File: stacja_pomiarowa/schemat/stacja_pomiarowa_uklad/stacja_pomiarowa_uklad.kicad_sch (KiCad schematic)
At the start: 24 parts, among them J1 Conn_02x17_Counter_Clockwise, J2 Conn_02x08_Counter_Clockwise, J3 Conn_01x01, J4 Conn_02x04_Counter_Clockwise, J5 Conn_01x02, J6 Conn_01x04, U1 CD4051B, U2 CD4051B, U3 ESP DevKitV1, U4 ADS1115, U5 CD4051B, U6 CD4051B, U7 MCP23017_SP, U8 4512

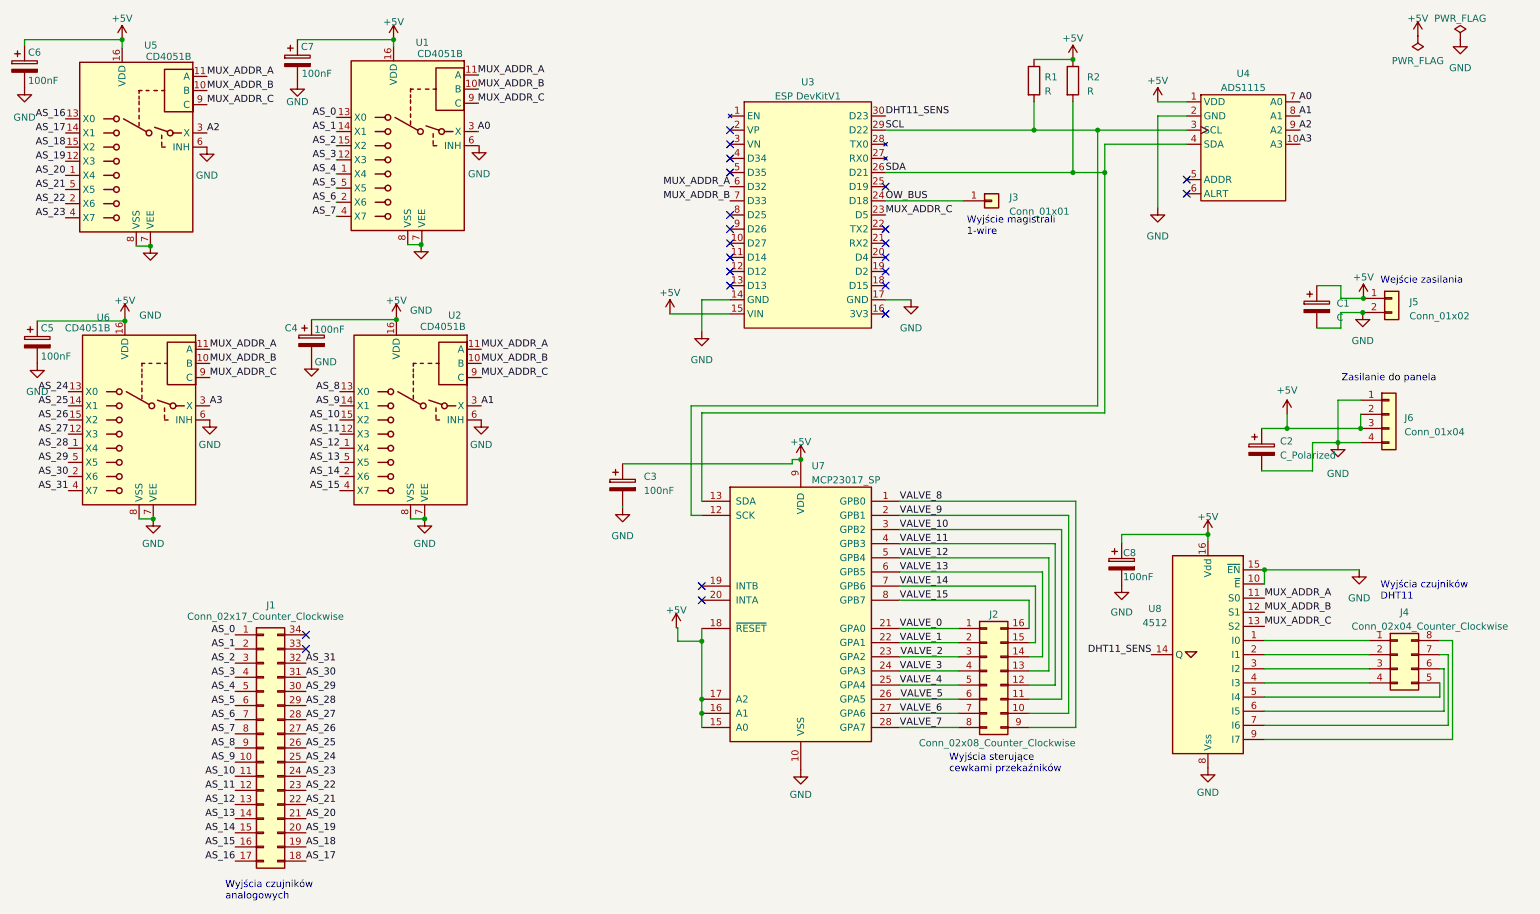
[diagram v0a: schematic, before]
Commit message: Poprawa schematu
Poprzednia numeracja wyjsc analogowych, dodany brakujacy tranzystor Q1, dodane brakujace oporniki podciagajace dla 1-wire i dht11, usuniete oporniki sciagajace dla wyjsc a[0..1] adc - w ten sposob przy niepodlaczonym czujniki nie bedzie stanu niskiego zamiast tego dodane oproniki sciagajace do zlacz dla czujnikow analogowych
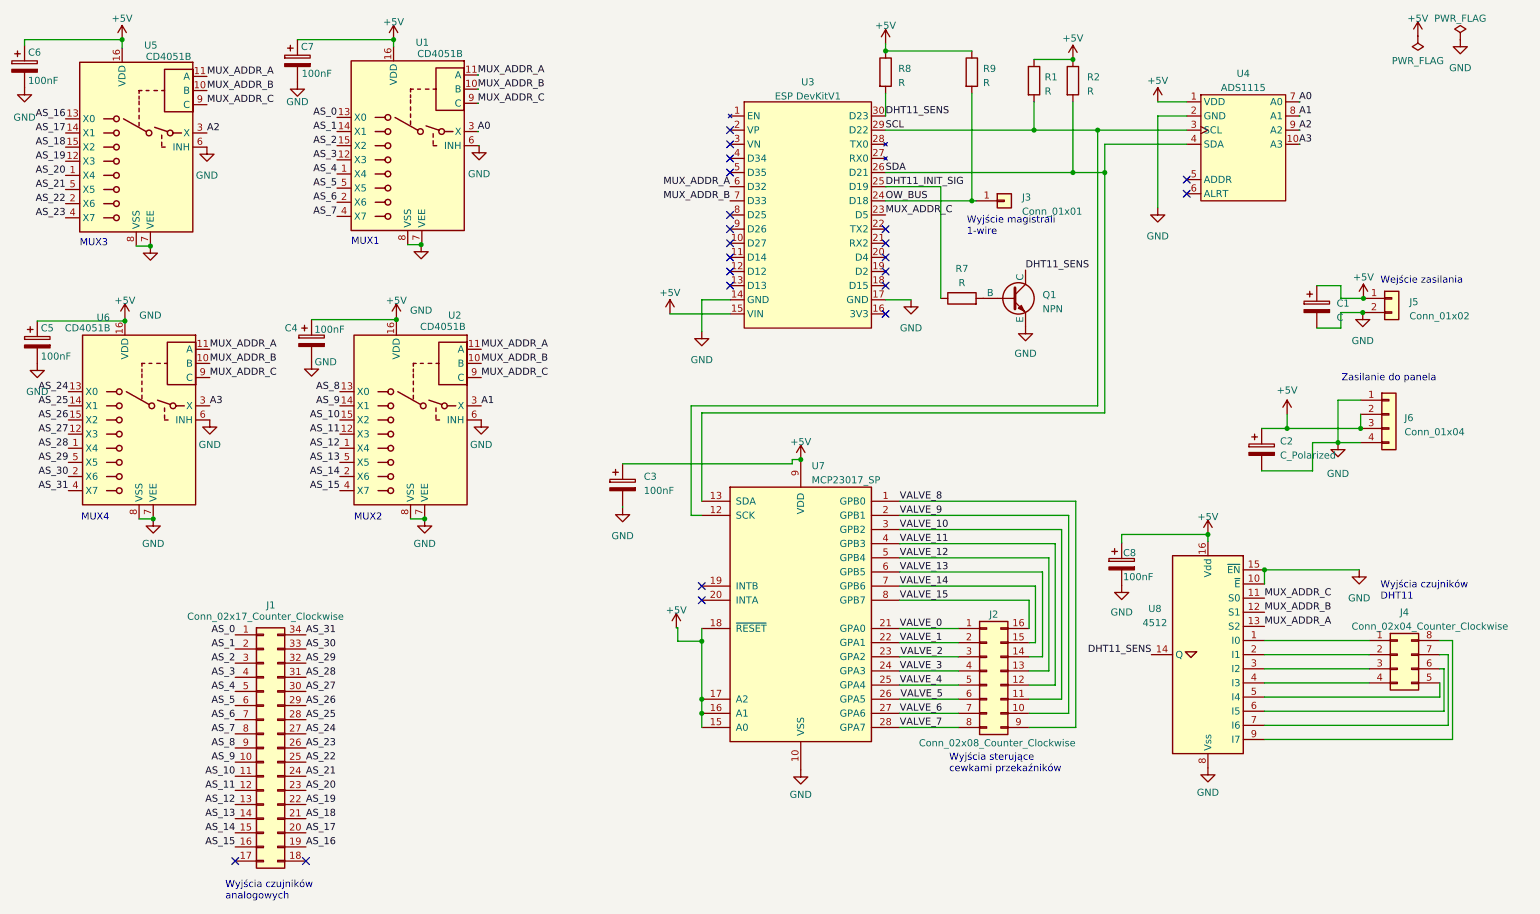
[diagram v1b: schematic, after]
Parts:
- added Q1: NPN, symbol Simulation_SPICE:NPN
- added R7, R8, R9: R, symbol Device:R
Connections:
- net +5V: now also R8.1, R9.1
- net AS_16: now also J1.19 (Pin_19); no longer J1.17 (Pin_17)
- net AS_17: now also J1.20 (Pin_20); no longer J1.18 (Pin_18)
- net AS_18: now also J1.21 (Pin_21); no longer J1.19 (Pin_19)
- net AS_19: now also J1.22 (Pin_22); no longer J1.20 (Pin_20)
- net AS_20: now also J1.23 (Pin_23); no longer J1.21 (Pin_21)
- net AS_21: now also J1.24 (Pin_24); no longer J1.22 (Pin_22)
- net AS_22: now also J1.25 (Pin_25); no longer J1.23 (Pin_23)
- net AS_23: now also J1.26 (Pin_26); no longer J1.24 (Pin_24)
- net AS_24: now also J1.27 (Pin_27); no longer J1.25 (Pin_25)
- net AS_25: now also J1.28 (Pin_28); no longer J1.26 (Pin_26)
- net AS_26: now also J1.29 (Pin_29); no longer J1.27 (Pin_27)
- net AS_27: now also J1.30 (Pin_30); no longer J1.28 (Pin_28)
- net AS_28: now also J1.31 (Pin_31); no longer J1.29 (Pin_29)
- net AS_29: now also J1.32 (Pin_32); no longer J1.30 (Pin_30)
- net AS_30: now also J1.33 (Pin_33); no longer J1.31 (Pin_31)
- net AS_31: now also J1.34 (Pin_34); no longer J1.32 (Pin_32)
- net DHT11_SENS: now also Q1.1 (C), R8.2
- net GND: now also Q1.3 (E)
- net MUX_ADDR_A: now also U8.13 (S2); no longer U8.11 (S0)
- net MUX_ADDR_C: now also U8.11 (S0); no longer U8.13 (S2)
- net OW_BUS: now also R9.2
- net DHT11_INIT_SIG: now reaches U3.25 (D19)
- net DHT11_INIT_SIG: now also R7.1
- new net: Q1.2 (B), R7.2
- no-connect marks 23 -> 22
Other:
- note added: "MUX1"
- note added: "MUX2"
- note added: "MUX3"
- note added: "MUX4"
- moved on the sheet: J3

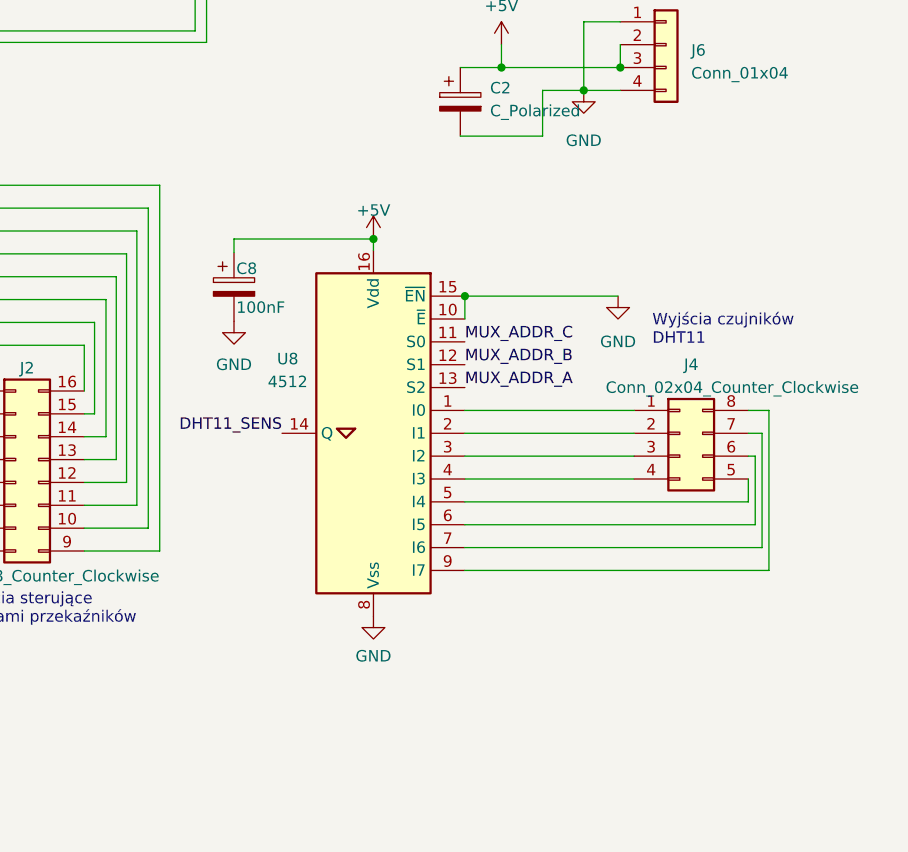
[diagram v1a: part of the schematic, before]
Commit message: Zmiana multipleksera 4512 na 4051
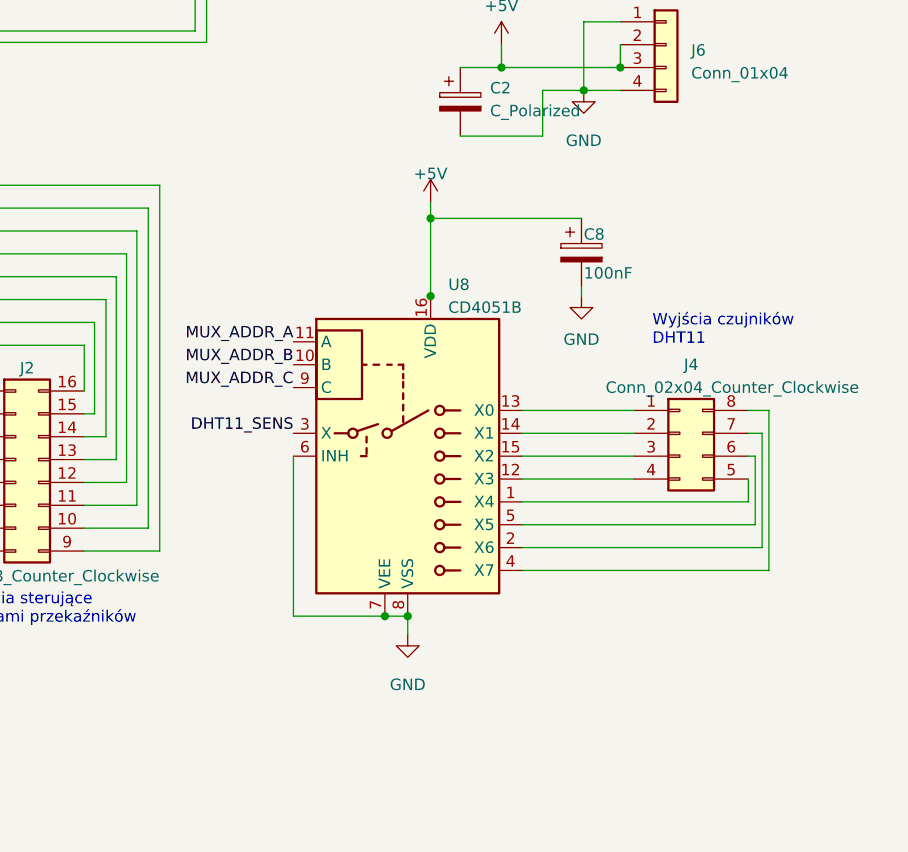
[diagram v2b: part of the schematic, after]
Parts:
- removed U8: 4512, Package_DIP:DIP-16_W7.62mm_Socket, symbol 4xxx_IEEE:4512
- added U8: CD4051B, symbol Analog_Switch:CD4051B
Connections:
- net +5V: now also U8.16 (VDD)
- net DHT11_SENS: now also U8.3 (X)
- net GND: now also U8.6 (INH), U8.7 (VEE), U8.8 (VSS)
- net MUX_ADDR_A: now also U8.11 (A)
- net MUX_ADDR_B: now also U8.10 (B)
- net MUX_ADDR_C: now also U8.9 (C)
- net at J4.1 (Pin_1): now also U8.13 (X0)
- net at J4.2 (Pin_2): now also U8.14 (X1)
- net at J4.3 (Pin_3): now also U8.15 (X2)
- net at J4.4 (Pin_4): now also U8.12 (X3)
- net at J4.5 (Pin_5): now also U8.1 (X4)
- net at J4.6 (Pin_6): now also U8.5 (X5)
- net at J4.7 (Pin_7): now also U8.2 (X6)
- net at J4.8 (Pin_8): now also U8.4 (X7)
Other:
- moved on the sheet: C8

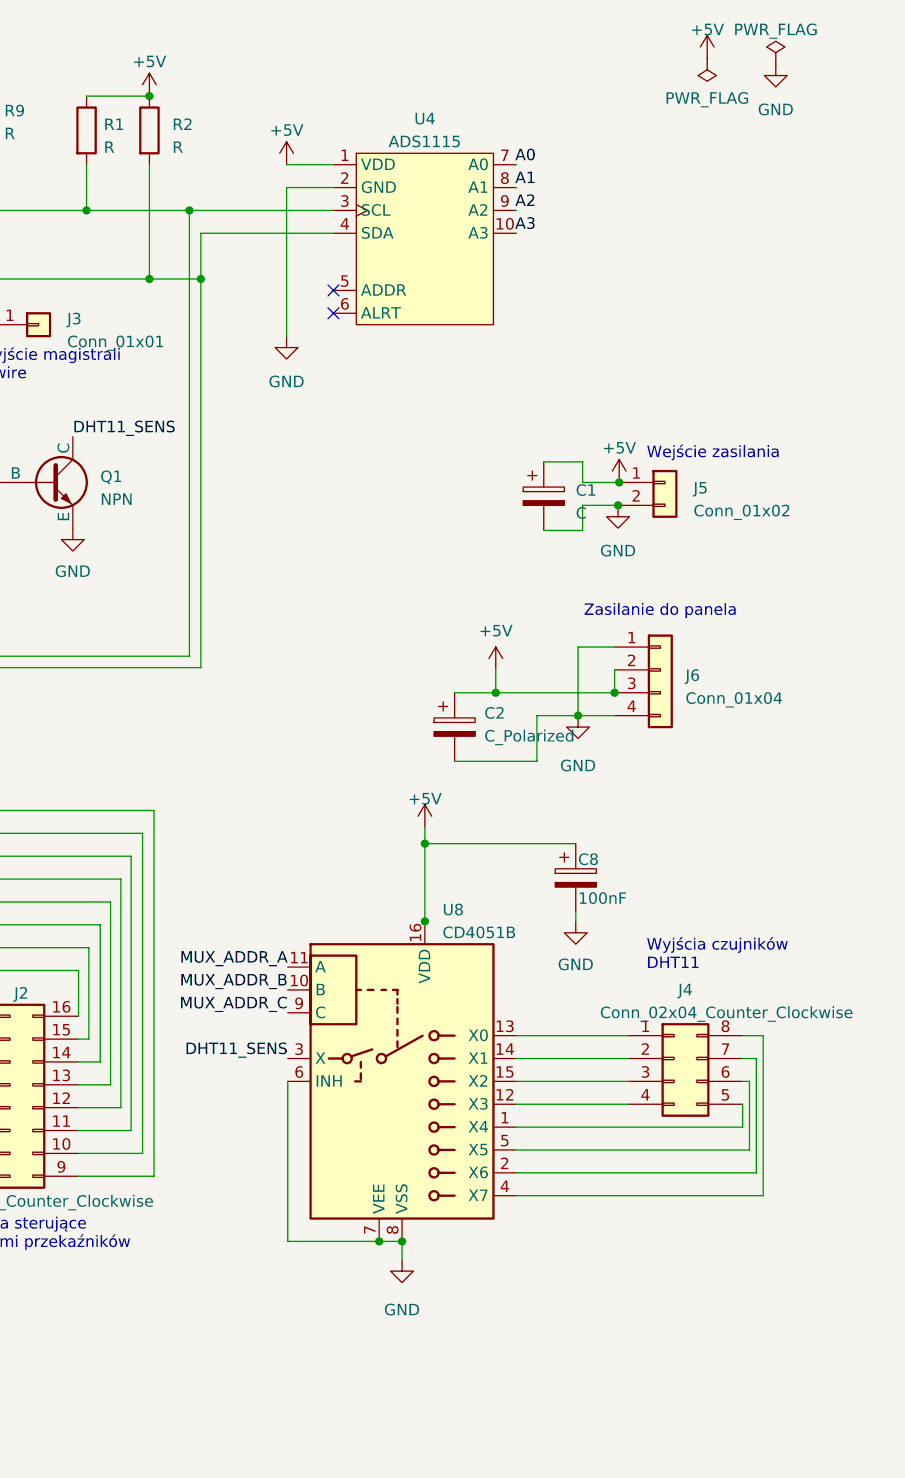
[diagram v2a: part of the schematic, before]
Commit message: Przywrócono oporniki do wejść ads1115, dodano brakujące oporniki do wejść multipleksera od dht11
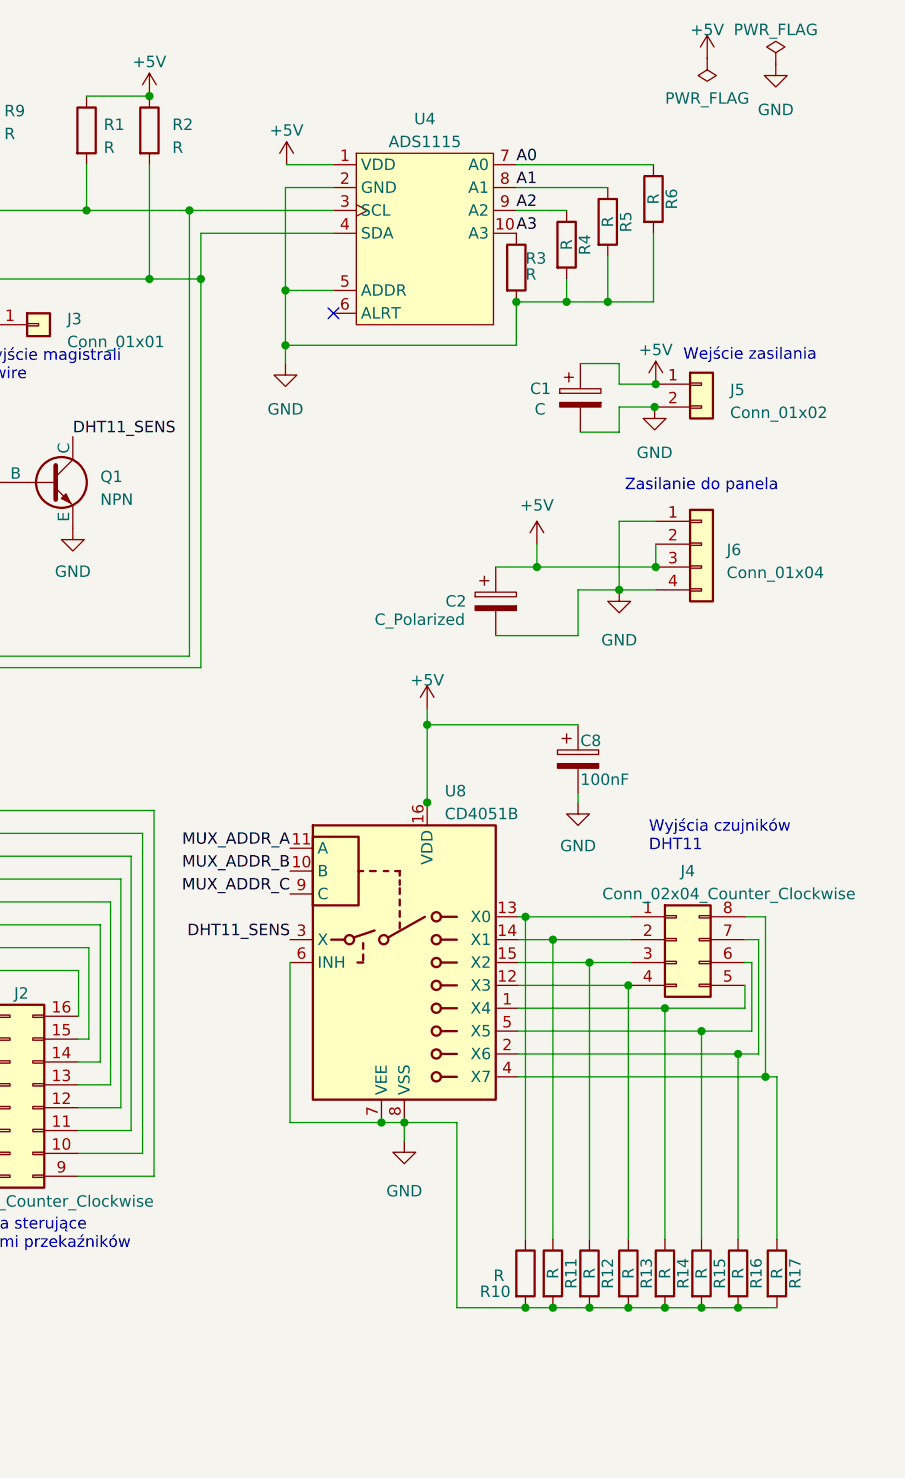
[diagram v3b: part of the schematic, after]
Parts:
- added R10, R11, R12, R13, R14, R15, R16, R17, R3, R4, R5, R6: R, symbol Device:R
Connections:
- net A0: now also R6.1
- net A1: now also R5.1
- net A2: now also R4.1
- net A3: now also R3.1
- net GND: now also U4.5 (ADDR), R10.2, R11.2, R12.2, R13.2, R14.2, R15.2, R16.2, R17.2, R3.2, R4.2, R5.2, R6.2
- net at J4.1 (Pin_1), U8.13 (X0): now also R10.1
- net at J4.2 (Pin_2), U8.14 (X1): now also R11.1
- net at J4.3 (Pin_3), U8.15 (X2): now also R12.1
- net at J4.4 (Pin_4), U8.12 (X3): now also R13.1
- net at J4.5 (Pin_5), U8.1 (X4): now also R14.1
- net at J4.6 (Pin_6), U8.5 (X5): now also R15.1
- net at J4.7 (Pin_7), U8.2 (X6): now also R16.1
- net at J4.8 (Pin_8), U8.4 (X7): now also R17.1
- no-connect marks 22 -> 21
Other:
- moved on the sheet: C1, C2, C8, J4, J5, J6, U8

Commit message: Zmiana złącza zasilania do panela z 4-pinowego na 2-pinowe
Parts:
- removed J6: Conn_01x04, Connector_Wire:SolderWire-2sqmm_1x04_P7.8mm_D2mm_OD3.9mm, symbol Connector_Generic:Conn_01x04
- added J6: Conn_01x02, symbol Connector_Generic:Conn_01x02
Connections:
- net +5V: now also J6.1 (Pin_1)
- net GND: now also J6.2 (Pin_2)
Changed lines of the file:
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@@
   (junction (at 256.286 49.276) (diameter 0) (color 0 0 0 0)
   )
-  (junction (at 261.62 78.74) (diameter 0) (color 0 0 0 0)
-  )
   (junction (at 258.572 161.036) (diameter 0) (color 0 0 0 0)
   )
@@
     (stroke (width 0) (type default))
   )
-  (wire (pts (xy 261.62 76.2) (xy 261.62 78.74))
-    (stroke (width 0) (type default))
-  )
   (wire (pts (xy 246.126 54.102) (xy 246.126 49.276))
     (stroke (width 0) (type default))
@@
     (stroke (width 0) (type default))
   )
-  (wire (pts (xy 257.556 73.66) (xy 261.62 73.66))
-    (stroke (width 0) (type default))
-  )
   (wire (pts (xy 138.684 128.651) (xy 138.684 130.937))
     (stroke (width 0) (type default))
@@
     (stroke (width 0) (type default))
   )
-  (wire (pts (xy 257.556 73.66) (xy 257.556 81.28))
-    (stroke (width 0) (type default))
-  )
   (wire (pts (xy 171.704 23.622) (xy 171.704 24.892))
     (stroke (width 0) (type default))
@@
     (effects (font (size 1.27 1.27)) (justify left bottom))
   )
-  (text "Zasilanie do panela" (at 258.191 70.485 0)
+  (text "Zasilanie do panela" (at 258.826 76.454 0)
     (effects (font (size 1.27 1.27)) (justify left bottom))
   )
@@
     )
   )
+  (symbol (lib_id "Connector_Generic:Conn_01x02") (at 266.7 78.74 0) (unit 1)
+    (in_bom yes) (on_board yes) (dnp no) (fields_autoplaced)
+    (property "Reference" "J6" (at 269.24 79.375 0)
+      (effects (font (size 1.27 1.27)) (justify left))
+    )
+    (property "Value" "Conn_01x02" (at 269.24 81.915 0)
+      (effects (font (size 1.27 1.27)) (justify left))
+    )
+    (property "Footprint" "" (at 266.7 78.74 0)
+      (effects (font (size 1.27 1.27)) hide)
+    )
+    (property "Datasheet" "~" (at 266.7 78.74 0)
+      (effects (font (size 1.27 1.27)) hide)
+    )
+    (pin "1")
+    (pin "2")
+    (instances
+      (project "stacja_pomiarowa_uklad"
+        (path "/634febf6-cc2f-434e-ad01-d800a8d45f65"
+          (reference "J6") (unit 1)
+        )
+      )
+    )
+  )
   (symbol (lib_id "Device:R") (at 246.126 45.466 0) (unit 1)
     (in_bom yes) (on_board yes) (dnp no)
@@
         )
       )
-    )
-  )
-  (symbol (lib_id "Connector_Generic:Conn_01x04") (at 266.7 76.2 0) (unit 1)
-    (in_bom yes) (on_board yes) (dnp no) (fields_autoplaced)
-    (property "Reference" "J6" (at 269.494 76.835 0)
-      (effects (font (size 1.27 1.27)) (justify left))
-    )
-    (property "Value" "Conn_01x04" (at 269.494 79.375 0)
-      (effects (font (size 1.27 1.27)) (justify left))
-    )
-    (property "Footprint" "Connector_Wire:SolderWire-2sqmm_1x04_P7.8mm_D2mm_OD3.9mm" (at 266.7 76.2 0)
-      (effects (font (size 1.27 1.27)) hide)
-    )
-    (property "Datasheet" "~" (at 266.7 76.2 0)
-      (effects (font (size 1.27 1.27)) hide)
-    )
-    (pin "1")
-    (pin "2")
-    (pin "3")
-    (pin "4")
-    (instances
-      (project "stacja_pomiarowa_uklad"
-        (path "/634febf6-cc2f-434e-ad01-d800a8d45f65"
-          (reference "J6") (unit 1)
-        )
-      )
